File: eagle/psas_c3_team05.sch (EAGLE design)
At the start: 92 parts, among them IC1 CP2102, J1 3220-10-0100-00, J2 1.27MM_HDR_2X12X1, U1 MIC5319 3.3V, U2 MCP73871, U3 MKW01Z128, X1 32 MHz

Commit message: fixed ground pads on MCU, generated new library that has everything in it
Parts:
- U3: device psas_c3:MKW01Z128 -> psas_c3_team05:MKW01Z128
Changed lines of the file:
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@@
 <part name="S1" library="Vibrogait_prototype" deviceset="SWITCH-SPST" device="PTH" value="EG1218"/>
 <part name="GND11" library="Vibrogait_prototype" deviceset="GND" device=""/>
-<part name="U3" library="psas_c3" deviceset="MKW01Z128" device="">
+<part name="U3" library="psas_c3_team05" deviceset="MKW01Z128" device="">
 <attribute name="DIST" value="Digi-Key"/>
 <attribute name="DPN" value="MKW01Z128CHN-ND"/>

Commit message: added some attributes to parts on sch/brd
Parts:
- U1: DIST (none) -> Digi-Key; DPN (none) -> 576-1910-1-ND; MFG (none) -> Microchip Technology; MFG-PN (none) -> MIC5319-3.3YD5-TR
- U3: MFG (none) -> Freescale Semiconductor; MFG-PN (none) -> MKW01Z128CHN; MFN Freescale Semiconductor -> (none); MPN MKW01Z128CHN -> (none)
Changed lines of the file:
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@@
 </classes>
 <parts>
-<part name="U1" library="Vibrogait_prototype" deviceset="SPARKFUN-POWERIC_V_REG_MIC5219" device="3.3V" value="MIC5319 3.3V"/>
+<part name="U1" library="Vibrogait_prototype" deviceset="SPARKFUN-POWERIC_V_REG_MIC5219" device="3.3V" value="MIC5319 3.3V">
+<attribute name="DIST" value="Digi-Key"/>
+<attribute name="DPN" value="576-1910-1-ND"/>
+<attribute name="MFG" value="Microchip Technology"/>
+<attribute name="MFG-PN" value="MIC5319-3.3YD5-TR"/>
+</part>
 <part name="JP1" library="Vibrogait_prototype" deviceset="SPARKFUN-CONNECTORS_M02" device="4UCON-15767" value="BC"/>
 <part name="GND1" library="Vibrogait_prototype" deviceset="GND" device=""/>
@@
 <attribute name="DIST" value="Digi-Key"/>
 <attribute name="DPN" value="MKW01Z128CHN-ND"/>
-<attribute name="MFN" value="Freescale Semiconductor"/>
-<attribute name="MPN" value="MKW01Z128CHN"/>
+<attribute name="MFG" value="Freescale Semiconductor"/>
+<attribute name="MFG-PN" value="MKW01Z128CHN"/>
 </part>
 <part name="GND13" library="Vibrogait_prototype" deviceset="GND" device=""/>
@@
 <attribute name="NAME" x="421.64" y="354.584" size="1.778" layer="95"/>
 <attribute name="VALUE" x="419.1" y="330.2" size="1.778" layer="96"/>
+<attribute name="DIST" x="429.26" y="345.44" size="1.778" layer="96" display="off"/>
+<attribute name="DPN" x="429.26" y="345.44" size="1.778" layer="96" display="off"/>
+<attribute name="MFG" x="429.26" y="345.44" size="1.778" layer="96" display="off"/>
+<attribute name="MFG-PN" x="429.26" y="345.44" size="1.778" layer="96" display="off"/>
 </instance>
 <instance part="JP1" gate="G$1" x="345.44" y="337.82" smashed="yes" rot="MR0">
@@
 <attribute name="DIST" x="241.3" y="185.42" size="1.778" layer="96" display="off"/>
 <attribute name="DPN" x="241.3" y="185.42" size="1.778" layer="96" display="off"/>
-<attribute name="MFN" x="241.3" y="185.42" size="1.778" layer="96" display="off"/>
-<attribute name="MPN" x="241.3" y="185.42" size="1.778" layer="96" display="off"/>
+<attribute name="MFG" x="241.3" y="185.42" size="1.778" layer="96" display="off"/>
+<attribute name="MFG-PN" x="241.3" y="185.42" size="1.778" layer="96" display="off"/>
 <attribute name="NAME" x="213.36" y="134.62" size="2.54" layer="95" font="vector" ratio="5"/>
 <attribute name="VALUE" x="213.36" y="132.08" size="2.54" layer="96" font="vector" ratio="5"/>

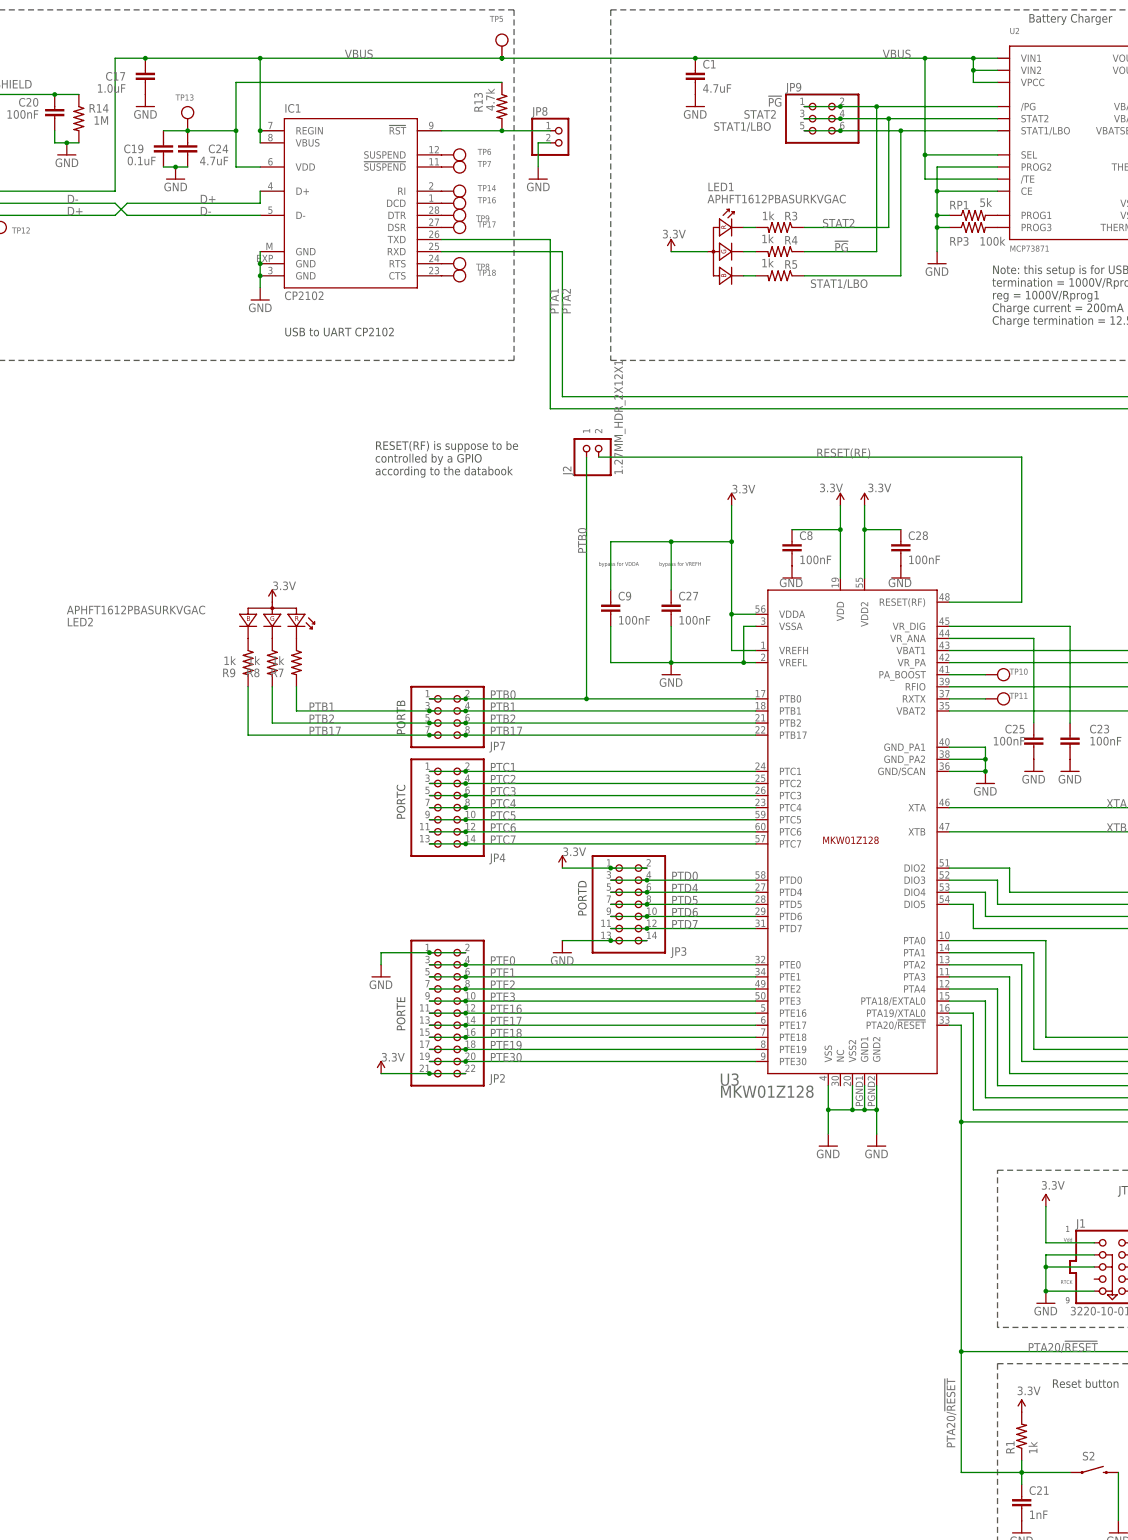
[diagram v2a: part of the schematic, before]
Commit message: Added part numbers for the voltage regulator and usb to uart
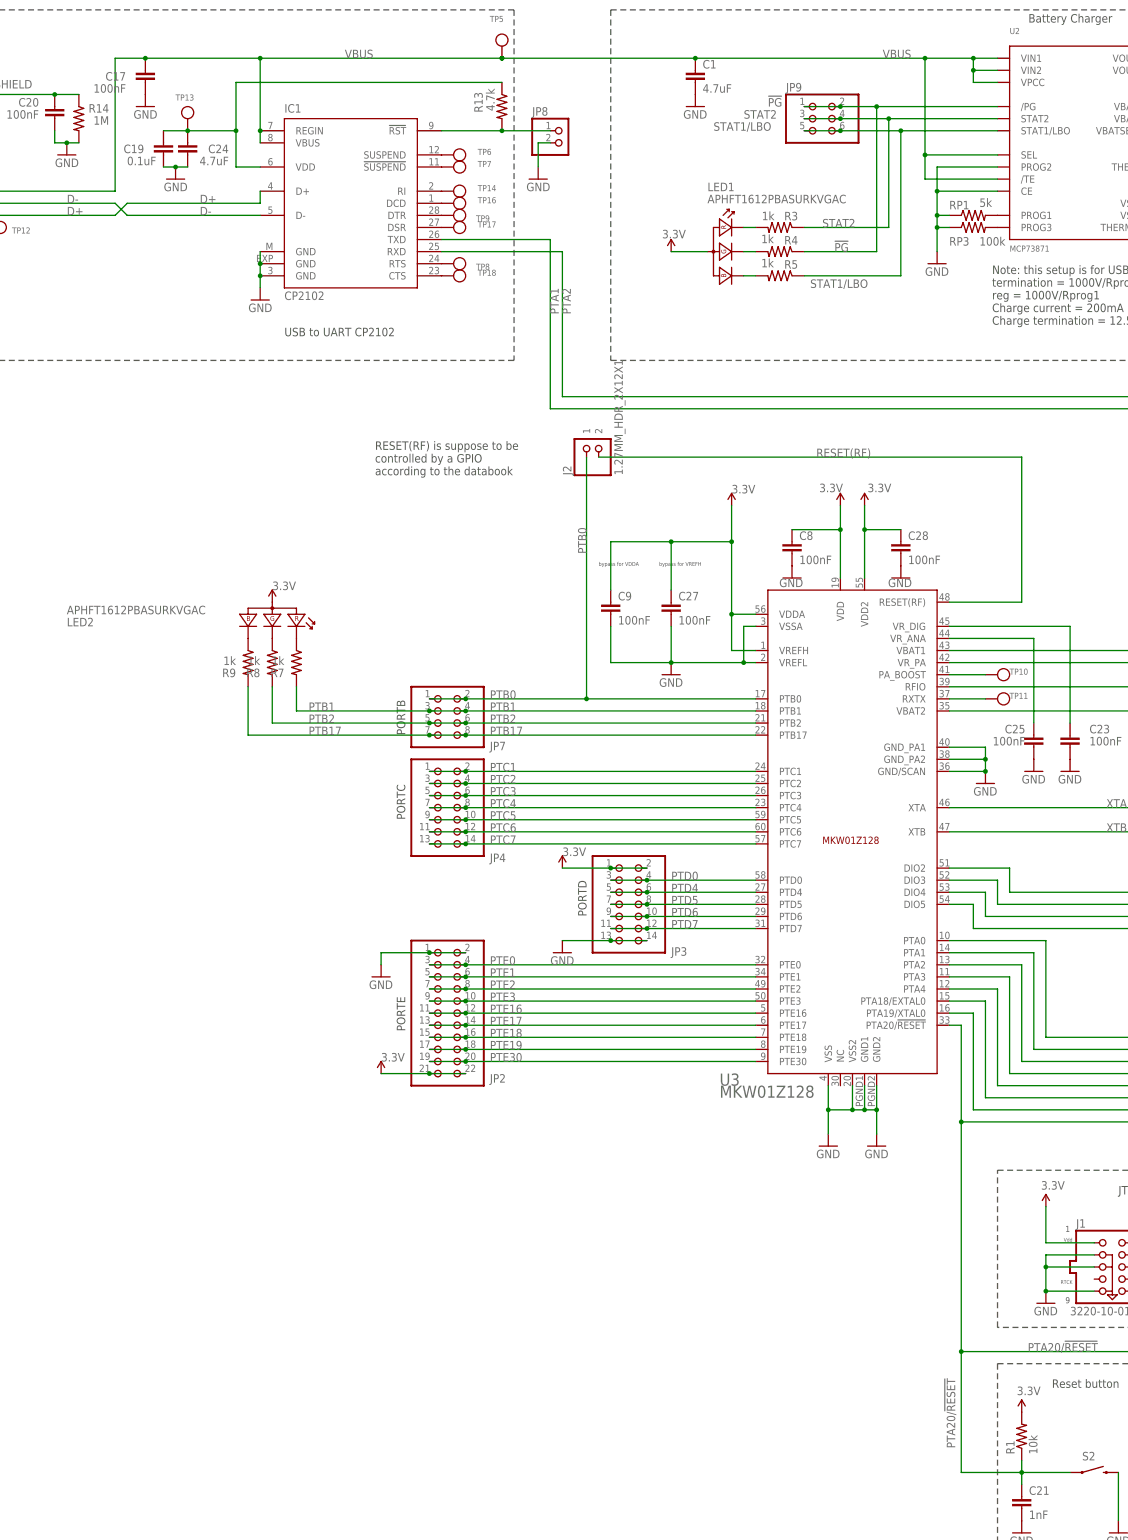
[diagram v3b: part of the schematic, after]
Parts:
- C1, C3, C4: DPN (none) -> 732-7657-1-ND
- C17: value 1.0uF -> 100nF; DIST (none) -> Digi-Key; DPN (none) -> 490-1532-1-ND
- C19, C20: DIST (none) -> Digi-Key; DPN (none) -> 490-1532-1-ND
- C24: DIST (none) -> Digi-Key; DPN (none) -> 732-7657-1-ND
- CF1: DIST (none) -> Digi-Key; DPN (none) -> H11610CT-ND
- LED1, LED2: DPN (none) -> 160-2022-1-ND
- R1: value 1k -> 10k
- R13: DPN (none) -> YAG1317CT-ND
- R14: DIST (none) -> Digi-Key; DPN (none) -> 311-1.00MHRCT-ND
- R3, R4, R5: DPN (none) -> 311-1.00KHRCT-ND
- RP1: DPN (none) -> YAG1305CT-ND
- RP3: DPN (none) -> 311-100KHRCT-ND
- RT1: DPN (none) -> 541-1151-1-ND

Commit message: more part nos
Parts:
- C2, C5, C7: DSN (none) -> 490-1532-1-ND
- RT1: DPN 541-1151-1-ND -> 480-3153-1-ND
- S1: DSN (none) -> EG1903-ND
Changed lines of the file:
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@@
 <part name="GND1" library="Vibrogait_prototype" deviceset="GND" device=""/>
 <part name="RT1" library="Vibrogait_prototype" deviceset="THERMISTOR-" device="_1206" value="10K (NTC)">
-<attribute name="DPN" value="541-1151-1-ND"/>
+<attribute name="DPN" value="480-3153-1-ND"/>
 </part>
 <part name="GND3" library="Vibrogait_prototype" deviceset="GND" device=""/>
@@
 <part name="SUPPLY1" library="supply2" deviceset="V+" device=""/>
 <part name="TP1" library="microbuilder" deviceset="TESTPOINT" device="ROUND0.5MM"/>
-<part name="C2" library="rcl_custom" deviceset="C-EU" device="0603-B-NOSILK" value="100nF"/>
+<part name="C2" library="rcl_custom" deviceset="C-EU" device="0603-B-NOSILK" value="100nF">
+<attribute name="DSN" value="490-1532-1-ND"/>
+</part>
 <part name="GND4" library="Vibrogait_prototype" deviceset="GND" device=""/>
 <part name="C3" library="rcl_custom" deviceset="C-EU" device="0805-B-NOSILK" value="4.7uF">
@@
 <part name="TP2" library="microbuilder" deviceset="TESTPOINT" device="ROUND0.5MM"/>
 <part name="TP3" library="microbuilder" deviceset="TESTPOINT" device="ROUND0.5MM"/>
-<part name="C5" library="rcl_custom" deviceset="C-EU" device="0603-B-NOSILK" value="100nF"/>
+<part name="C5" library="rcl_custom" deviceset="C-EU" device="0603-B-NOSILK" value="100nF">
+<attribute name="DSN" value="490-1532-1-ND"/>
+</part>
 <part name="C6" library="rcl_custom" deviceset="C-EU" device="0805-B-NOSILK" value="2.2uF"/>
-<part name="C7" library="rcl_custom" deviceset="C-EU" device="0603-B-NOSILK" value="100nF"/>
+<part name="C7" library="rcl_custom" deviceset="C-EU" device="0603-B-NOSILK" value="100nF">
+<attribute name="DSN" value="490-1532-1-ND"/>
+</part>
 <part name="GND7" library="Vibrogait_prototype" deviceset="GND" device=""/>
 <part name="GND8" library="Vibrogait_prototype" deviceset="GND" device=""/>
@@
 <part name="TP4" library="microbuilder" deviceset="TESTPOINT" device="ROUND0.5MM"/>
 <part name="GND10" library="Vibrogait_prototype" deviceset="GND" device=""/>
-<part name="S1" library="Vibrogait_prototype" deviceset="SWITCH-SPST" device="PTH" value="EG1218"/>
+<part name="S1" library="Vibrogait_prototype" deviceset="SWITCH-SPST" device="PTH" value="EG1218">
+<attribute name="DSN" value="EG1903-ND"/>
+</part>
 <part name="GND11" library="Vibrogait_prototype" deviceset="GND" device=""/>
 <part name="U3" library="psas_c3_team05" deviceset="MKW01Z128" device="">
@@
 <attribute name="NAME" x="392.684" y="348.361" size="1.778" layer="95"/>
 <attribute name="VALUE" x="392.684" y="343.281" size="1.778" layer="96"/>
+<attribute name="DSN" x="391.16" y="347.98" size="1.778" layer="96" display="off"/>
 </instance>
 <instance part="GND4" gate="1" x="391.16" y="332.74" smashed="yes">
@@
 <attribute name="NAME" x="451.104" y="345.821" size="1.778" layer="95"/>
 <attribute name="VALUE" x="451.104" y="340.741" size="1.778" layer="96"/>
+<attribute name="DSN" x="449.58" y="345.44" size="1.778" layer="96" display="off"/>
 </instance>
 <instance part="C6" gate="CE" x="464.82" y="345.44" smashed="yes">
@@
 <attribute name="NAME" x="440.944" y="338.201" size="1.778" layer="95"/>
 <attribute name="VALUE" x="440.944" y="333.121" size="1.778" layer="96"/>
+<attribute name="DSN" x="439.42" y="337.82" size="1.778" layer="96" display="off"/>
 </instance>
 <instance part="GND7" gate="1" x="439.42" y="327.66" smashed="yes">
@@
 <attribute name="NAME" x="408.94" y="335.28" size="1.778" layer="95"/>
 <attribute name="VALUE" x="408.94" y="332.74" size="1.778" layer="96"/>
+<attribute name="DSN" x="416.56" y="340.36" size="1.778" layer="96" rot="R180" display="off"/>
 </instance>
 <instance part="GND11" gate="1" x="317.5" y="330.2" smashed="yes">
